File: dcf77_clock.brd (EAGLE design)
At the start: 83.1 x 76.2 mm, 42 parts, among them IC1 7805DT, IC2 ATMEGA48/88/168-AU, J2 DCJ0202, Q1 32.768kHz, Q2 IRLML6244TRPBF, SW1 EC12E_SW, U1 LCD-16X2SILK, U2 DS1307SO8

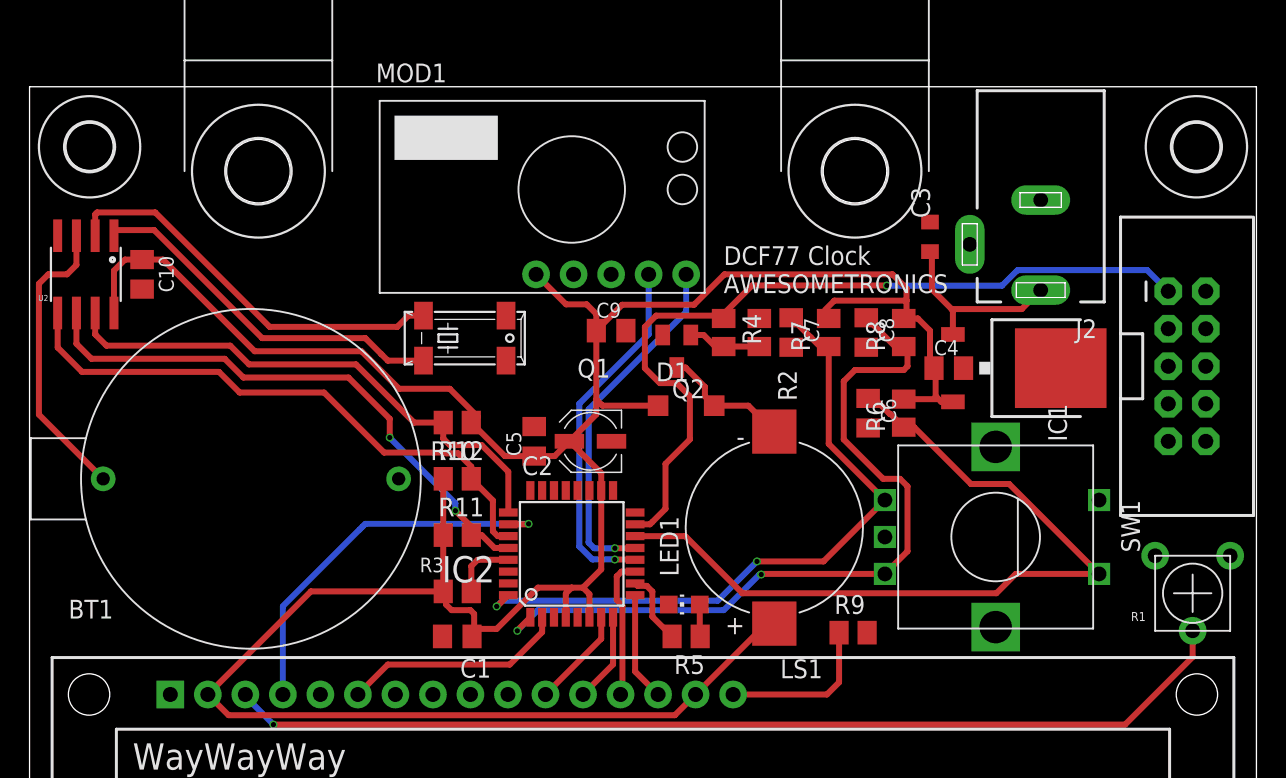
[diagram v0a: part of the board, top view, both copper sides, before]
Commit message: Finish signal and VCC routing
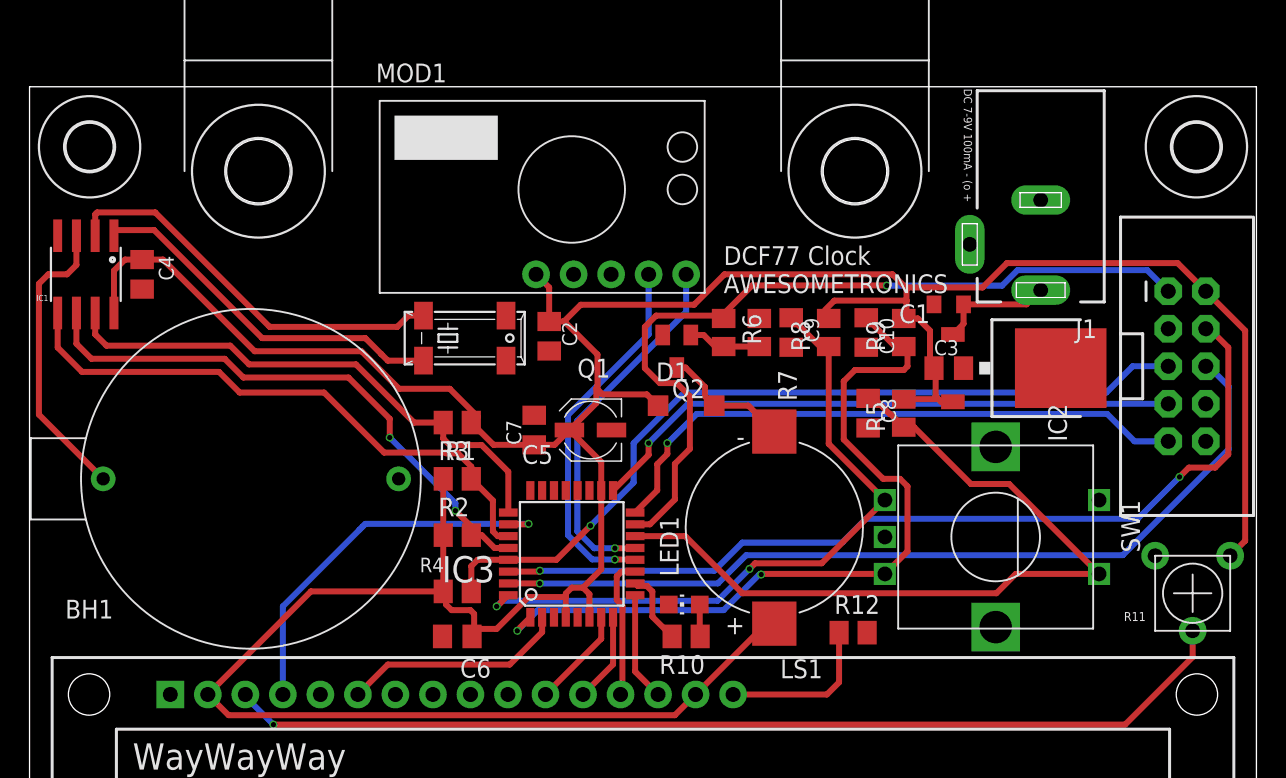
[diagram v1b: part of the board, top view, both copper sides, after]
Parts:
- removed U$1: AVR_SPI_PROG2PTH2, SparkFun:2X5-SHROUDED
- added IC3: ATMEGA48/88/168-AU, atmega8:TQFP32-08
- C1: value 100n -> 0.22uF; device rcl:C0805K -> rcl:SMC_Z
- C2: value 22uF -> 100n; device rcl:UD-4X5,8_NICHICON -> rcl:C0805K
- C3: value 0.22uF -> 100n; device rcl:SMC_Z -> rcl:C0805K
- C5: value 100n -> 22uF; device rcl:C0805K -> rcl:UD-4X5,8_NICHICON
- IC1: value 7805DT -> DS1307SO8; device linear:TO252 -> SparkFun:SO08
- IC2: value ATMEGA48/88/168-AU -> 7805DT; device atmega8:TQFP32-08 -> linear:TO252
- R1: value 10k -> 4.7k; device SparkFun:TRIM_POT_PTH -> rcl:M0805
- R10, R12: value 4.7k -> 100R
- R11: value 4.7k -> 10k; device rcl:M0805 -> SparkFun:TRIM_POT_PTH
- R2, R3: value 10k -> 4.7k
- R4: value 1k -> 10k
- R5, R9: value 100R -> 10k
- R6: value 10k -> 1k
- U1: value LCD-16X2SILK -> AVR_SPI_PROG2PTH2; device SparkFun:LCD-16X2 -> SparkFun:2X5-SHROUDED
- U2: value DS1307SO8 -> LCD-16X2SILK; device SparkFun:SO08 -> SparkFun:LCD-16X2
- moved IC1 63.8 mm to (3.81, 63.5), turned to 180 degrees
- moved U2 57.9 mm to (41.5, 19.6), turned to 0 degrees
- moved C4 55.0 mm to (7.62, 63.5), turned to 270 degrees
- moved U1 52.7 mm to (78.4, 57.3)
- moved R1 51.1 mm to (29.0, 53.5)
- moved R11 49.9 mm to (78.7, 41.9), turned to 180 degrees
- moved C10 49.2 mm to (56.6, 59.6)
- moved HOLD1 40.4 mm to (55.9, 70.5)
- moved HOLD2 40.4 mm to (15.5, 70.5)
- moved C1 40.2 mm to (62.2, 61.5)
- moved IC2 33.1 mm to (67.3, 57.1), turned to 270 degrees
- moved C6 31.7 mm to (29.0, 39.0), turned to 180 degrees
- moved R12 28.7 mm to (55.8, 39.2)
- moved R4 25.1 mm to (29.0, 42.0), turned to 0 degrees
- moved R2 24.6 mm to (29.0, 45.8), turned to 0 degrees
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- renumbered BT1 to BH1, J2 to J1
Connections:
- net DCF77_OUT: now also IC3.12; no longer IC2.12
- net DCF77_SEL: now also IC3.13; no longer IC2.13
- net ENC_A: now also C9.1, IC3.32, R8.1; no longer C7.1, IC2.32, R7.1
- net ENC_B: now also C10.1, IC3.1, R9.1; no longer C8.1, IC2.1, R8.1
- net GND: now also C1.-, C2.2, C3.2, C5.-, IC1.4, IC3.21, IC3.3, IC3.5, R11.3, R12.2, R7.1, U1.10, U1.8, U2.1, U2.5; no longer C1.2, C2.-, C3.-, C5.2, IC1.3, IC2.21, IC2.5, R1.3, R2.1, R9.2, U$1.10, U$1.8, U1.1, U1.5, U2.4
- net ISP_MISO: now also IC3.16, U1.9; no longer IC2.16, U$1.9
- net ISP_MOSI_BUZ_PWM: now also IC3.15, R6.1, U1.1; no longer IC2.15, R4.1, U$1.1
- net ISP_SCK: now also IC3.17, U1.7; no longer IC2.17, U$1.7
- net LCD_DB4: now also IC3.7, U2.11; no longer IC2.7, U1.11
- net LCD_DB5: now also IC3.8, U2.12; no longer IC2.8, U1.12
- net LCD_DB6: now also IC3.11, U2.13; no longer IC2.11, U1.13
- net LCD_DB7: now also IC3.9, U2.14; no longer IC2.9, U1.14
- net LCD_E: now also IC3.2, U2.6; no longer IC2.2, U1.6
- net LCD_RS: now also IC3.26, U2.4; no longer IC2.26, U1.4
- net LED: now also IC3.10, R10.2; no longer IC2.10, R5.2
- net MCU_RX: now also IC3.30, U1.4; no longer IC2.30, U$1.4
- net MCU_TX: now also IC3.31, U1.6; no longer IC2.31, U$1.6
- net N$1: now also C1.+, IC2.1; no longer C3.+, IC1.1
- net N$10: now also IC1.1; no longer U2.1
- net N$11: now also IC1.2; no longer U2.2
- net N$12: now also IC1.3; no longer U2.3
- net N$3: now also R6.2, R7.2; no longer R2.2, R4.2
- net N$4: now also R10.1; no longer R5.1
- net N$7: now also R11.2, U2.3; no longer R1.2, U1.3
- net N$9: now also R12.1, U2.16; no longer R9.1, U1.16
- net RESET: now also IC3.29, R4.2, U1.5; no longer IC2.29, R3.2, U$1.5
- net RTC_SCL: now also IC1.6, IC3.28, R2.2; no longer IC2.28, R11.2, U2.6
- net RTC_SDA: now also IC1.5, IC3.27, R3.2; no longer IC2.27, R12.2, U2.5
- net RTC_SQW: now also IC1.7, IC3.25, R1.2; no longer IC2.25, R10.2, U2.7
- net SW: now also C8.1, IC3.14, R5.1; no longer C6.1, IC2.14, R6.1
- net VCC: now also C2.1, C3.1, C5.+, C6.1, C7.1, IC1.8, IC2.2, IC3.18, IC3.4, IC3.6, R2.1, R4.1, R5.2, R9.2, U2.15, U2.2; no longer C1.1, C10.1, C2.+, C5.1, C9.1, IC1.2, IC2.18, IC2.4, IC2.6, R10.1, R12.1, R6.2, R7.2, U$1.2, U1.15, U2.8
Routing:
- net MCU_RX: track 0.00 -> 61.3 mm, vias 0 -> 2
- net MCU_TX: track 0.00 -> 58.9 mm, vias 0 -> 1
- net RESET: track 4.39 -> 56.1 mm, vias 0 -> 1
- net VCC: track 198.3 -> 240.7 mm
- net ISP_MISO: track 0.00 -> 41.1 mm, vias 0 -> 1
- net ISP_SCK: track 0.00 -> 40.5 mm, vias 0 -> 1
- net N$1: track 12.8 -> 7.96 mm
- net DCF77_OUT: track 24.5 -> 25.2 mm
- net DCF77_SEL: track 24.3 -> 24.9 mm
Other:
- board text added: "DC 7-9V 100mA - (o +"

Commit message: Add BOM
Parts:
- U2: value LCD-16X2SILK -> LCD-16X2UPPERHOLES; device SparkFun:LCD-16X2 -> dcf77:LCD-16X2_UPPER_HOLES
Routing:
- net N$7: track 68.7 -> 68.1 mm

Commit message: Add GND polygon and missing vias
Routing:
- net VCC: track 240.8 -> 241.5 mm
- added copper zone on layer 1, net GND
- added copper zone on layer 16, net GND
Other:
- board text added: "DC 7-9V 100mA"
- board text removed: "DC 7-9V 100mA - (o +"
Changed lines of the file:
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@@
 <dimension x1="10.541" y1="88.9" x2="60.96" y2="88.9" x3="35.7505" y3="97.79" textsize="1.778" layer="1"/>
 <text x="6.985" y="29.972" size="1.778" layer="25">WayWayWay</text>
-<text x="63.246" y="76.073" size="0.5588" layer="25" rot="SR270">DC 7-9V 100mA - (o +</text>
+<text x="63.246" y="76.073" size="0.5588" layer="25" rot="SR270">DC 7-9V 100mA</text>
+<wire x1="63.5" y1="70.1802" x2="63.5" y2="69.9262" width="0.1016" layer="25"/>
+<wire x1="63.373" y1="68.9102" x2="63.5" y2="68.9102" width="0.1016" layer="25"/>
+<wire x1="63.5" y1="68.9102" x2="63.627" y2="68.9102" width="0.1016" layer="25"/>
+<wire x1="63.5" y1="68.9102" x2="63.5" y2="68.7832" width="0.1016" layer="25"/>
+<wire x1="63.5" y1="68.9102" x2="63.5" y2="69.0372" width="0.1016" layer="25"/>
+<wire x1="63.1698" y1="69.4182" x2="63.8048" y2="69.4182" width="0.1016" layer="25" curve="-180"/>
+<circle x="63.5" y="69.4182" radius="0.127" width="0.1016" layer="25"/>
 </plain>
 <attributes>
@@
 <contactref element="C2" pad="2"/>
 <contactref element="C4" pad="2"/>
-<wire x1="63.653" y1="65.532" x2="68.453" y2="68.532" width="0" layer="19" extent="1-1"/>
-<wire x1="61.23" y1="61.468" x2="63.653" y2="65.532" width="0" layer="19" extent="1-1"/>
-<wire x1="63.23" y1="57.15" x2="61.23" y2="61.468" width="0" layer="19" extent="1-1"/>
-<wire x1="56.642" y1="58.563" x2="61.23" y2="61.468" width="0" layer="19" extent="1-1"/>
-<wire x1="51.562" y1="58.563" x2="56.642" y2="58.563" width="0" layer="19" extent="1-1"/>
-<wire x1="49.403" y1="60.513" x2="51.562" y2="58.563" width="0" layer="19" extent="1-1"/>
-<wire x1="56.769" y1="53.102" x2="56.642" y2="58.563" width="0" layer="19" extent="1-1"/>
-<wire x1="69.81" y1="57.15" x2="63.23" y2="57.15" width="0" layer="19" extent="1-1"/>
-<wire x1="42.865" y1="59.393" x2="49.403" y2="60.513" width="0" layer="19" extent="1-1"/>
-<wire x1="36.83" y1="63.5" x2="42.865" y2="59.393" width="0" layer="19" extent="1-1"/>
-<wire x1="35.179" y1="58.309" x2="36.83" y2="63.5" width="0" layer="19" extent="1-1"/>
-<wire x1="34.163" y1="53.959" x2="35.179" y2="58.309" width="0" layer="19" extent="1-1"/>
-<wire x1="39.398" y1="52.959" x2="34.163" y2="53.959" width="0" layer="19" extent="1-1"/>
-<wire x1="36.303" y1="48.8696" x2="39.398" y2="52.959" width="0" layer="19" extent="1-1"/>
-<wire x1="57.905" y1="45.72" x2="56.769" y2="53.102" width="0" layer="19" extent="1-1"/>
-<wire x1="56.703" y1="39.243" x2="57.905" y2="45.72" width="0" layer="19" extent="1-1"/>
-<wire x1="37.103" y1="40.2844" x2="36.303" y2="48.8696" width="0" layer="19" extent="1-1"/>
-<wire x1="35.503" y1="40.2844" x2="37.103" y2="40.2844" width="0" layer="19" extent="1-1"/>
-<wire x1="43.273" y1="41.148" x2="37.103" y2="40.2844" width="0" layer="19" extent="1-1"/>
-<wire x1="27.956" y1="38.989" x2="35.503" y2="40.2844" width="0" layer="19" extent="1-1"/>
-<wire x1="19.689" y1="35.058" x2="27.956" y2="38.989" width="0" layer="19" extent="1-1"/>
-<wire x1="72.405" y1="48.22" x2="69.81" y2="57.15" width="0" layer="19" extent="1-1"/>
-<wire x1="76.2" y1="44.45" x2="72.405" y2="48.22" width="0" layer="19" extent="1-1"/>
-<wire x1="79.629" y1="52.197" x2="72.405" y2="48.22" width="0" layer="19" extent="1-1"/>
-<wire x1="79.629" y1="54.737" x2="79.629" y2="52.197" width="0" layer="19" extent="1-1"/>
-<wire x1="24.986" y1="49.657" x2="34.163" y2="53.959" width="0" layer="19" extent="1-1"/>
-<wire x1="9.529" y1="35.058" x2="19.689" y2="35.058" width="0" layer="19" extent="1-1"/>
-<wire x1="7.62" y1="62.5" x2="24.986" y2="49.657" width="0" layer="19" extent="1-1"/>
-<wire x1="1.905" y1="66.1162" x2="7.62" y2="62.5" width="0" layer="19" extent="1-1"/>
+<polygon width="0.2032" layer="1" isolate="0.2032">
+<vertex x="-2.54" y="80.01"/>
+<vertex x="85.09" y="80.01"/>
+<vertex x="85.09" y="-2.54"/>
+<vertex x="-2.54" y="-2.54"/>
+</polygon>
+<polygon width="0.3048" layer="16" isolate="0.3048">
+<vertex x="-3.81" y="82.55"/>
+<vertex x="88.9" y="82.55"/>
+<vertex x="88.9" y="-8.89"/>
+<vertex x="-12.7" y="-8.89"/>
+<vertex x="-12.7" y="82.55"/>
+</polygon>
+<via x="35.56" y="38.481" extent="1-16" drill="0.35"/>
+<via x="36.576" y="38.481" extent="1-16" drill="0.35"/>
+<via x="33.782" y="36.83" extent="1-16" drill="0.35"/>
+<via x="35.052" y="36.83" extent="1-16" drill="0.35"/>
+<via x="24.13" y="40.64" extent="1-16" drill="0.35"/>
+<via x="25.4" y="40.64" extent="1-16" drill="0.35"/>
+<via x="22.86" y="39.37" extent="1-16" drill="0.35"/>
+<via x="24.257" y="39.37" extent="1-16" drill="0.35"/>
+<via x="25.527" y="39.37" extent="1-16" drill="0.35"/>
+<via x="30.607" y="55.88" extent="1-16" drill="0.35"/>
+<via x="31.75" y="55.88" extent="1-16" drill="0.35"/>
+<via x="33.02" y="55.88" extent="1-16" drill="0.35"/>
+<via x="34.29" y="55.88" extent="1-16" drill="0.35"/>
+<via x="35.56" y="55.88" extent="1-16" drill="0.35"/>
+<via x="39.751" y="51.308" extent="1-16" drill="0.35"/>
+<via x="39.751" y="50.419" extent="1-16" drill="0.35"/>
+<via x="40.894" y="54.229" extent="1-16" drill="0.35"/>
+<via x="48.26" y="56.515" extent="1-16" drill="0.35"/>
+<via x="49.53" y="56.515" extent="1-16" drill="0.35"/>
+<via x="50.8" y="56.515" extent="1-16" drill="0.35"/>
+<via x="52.07" y="56.515" extent="1-16" drill="0.35"/>
+<via x="55.245" y="57.531" extent="1-16" drill="0.35"/>
+<via x="55.372" y="59.563" extent="1-16" drill="0.35"/>
+<via x="60.198" y="61.722" extent="1-16" drill="0.35"/>
+<via x="62.23" y="60.579" extent="1-16" drill="0.35"/>
+<via x="42.291" y="44.704" extent="1-16" drill="0.35"/>
+<via x="43.561" y="44.704" extent="1-16" drill="0.35"/>
+<via x="51.054" y="61.849" extent="1-16" drill="0.35"/>
+<via x="52.578" y="61.849" extent="1-16" drill="0.35"/>
+<via x="33.782" y="50.292" extent="1-16" drill="0.35"/>
+<via x="34.671" y="50.292" extent="1-16" drill="0.35"/>
+<via x="35.433" y="50.292" extent="1-16" drill="0.35"/>
+<via x="57.785" y="51.435" extent="1-16" drill="0.35"/>
+<via x="59.69" y="51.435" extent="1-16" drill="0.35"/>
+<via x="60.452" y="50.673" extent="1-16" drill="0.35"/>
+<via x="61.341" y="49.911" extent="1-16" drill="0.35"/>
+<via x="62.357" y="49.022" extent="1-16" drill="0.35"/>
+<via x="60.96" y="45.72" extent="1-16" drill="0.35"/>
+<via x="63.5" y="45.72" extent="1-16" drill="0.35"/>
+<via x="65.405" y="45.72" extent="1-16" drill="0.35"/>
 </signal>
 <signal name="VCC">
@@
 <wire x1="59.182" y1="55.052" x2="61.402" y2="55.052" width="0.508" layer="1"/>
 <wire x1="61.402" y1="55.052" x2="61.468" y2="55.118" width="0.4064" layer="1"/>
-<wire x1="54.483" y1="61.722" x2="53.848" y2="61.087" width="0.4064" layer="1"/>
+<wire x1="53.848" y1="61.087" x2="54.483" y2="61.722" width="0.4064" layer="1"/>
 <wire x1="60.96" y1="59.69" x2="60.137" y2="60.513" width="0.508" layer="1"/>
 <wire x1="60.137" y1="60.513" x2="59.309" y2="60.513" width="0.4064" layer="1"/>
@@
 <wire x1="82.296" y1="45.466" x2="81.28" y2="44.45" width="0.4064" layer="1"/>
 <wire x1="82.296" y1="59.69" x2="82.296" y2="45.466" width="0.4064" layer="1"/>
-<wire x1="53.848" y1="61.087" x2="54.102" y2="60.513" width="0" layer="19" extent="1-1"/>
+<wire x1="54.102" y1="60.513" x2="53.848" y2="60.767" width="0.3048" layer="1"/>
+<wire x1="53.848" y1="60.767" x2="53.848" y2="61.087" width="0.3048" layer="1"/>
 </signal>
 <signal name="N$1">
@@
 <wire x1="43.688" y1="48.26" x2="43.688" y2="50.673" width="0.4064" layer="1"/>
 <wire x1="43.688" y1="50.673" x2="44.704" y2="51.689" width="0.4064" layer="1"/>
-<wire x1="48.92070625" y1="62.7506" x2="46.99" y2="60.81989375" width="0.4064" layer="1"/>
+<wire x1="46.99" y1="60.81989375" x2="48.92070625" y2="62.7506" width="0.4064" layer="1"/>
 <wire x1="40.9956" y1="46.577" x2="42.005" y2="46.577" width="0.4064" layer="1"/>
-<wire x1="46.99" y1="60.513" x2="46.99" y2="60.81989375" width="0" layer="19" extent="1-1"/>
+<wire x1="46.99" y1="60.513" x2="46.99" y2="60.81989375" width="0.3048" layer="1"/>
 </signal>
 <signal name="ISP_MISO">
@@
 <wire x1="29.083" y1="51.308" x2="29.906" y2="50.485" width="0.4064" layer="1"/>
 </signal>
+<signal name="N$14">
+<via x="42.418" y="37.084" extent="1-16" drill="0.35"/>
+</signal>
+<signal name="N$15">
+<via x="43.942" y="37.084" extent="1-16" drill="0.35"/>
+</signal>
 </signals>

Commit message: Place hidden encoder pins and connect to GND
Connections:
- net GND: now also SW1.GND1, SW1.GND2
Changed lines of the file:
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@@
 <via x="63.5" y="45.72" extent="1-16" drill="0.35"/>
 <via x="65.405" y="45.72" extent="1-16" drill="0.35"/>
+<contactref element="SW1" pad="GND2"/>
+<contactref element="SW1" pad="GND1"/>
 </signal>
 <signal name="VCC">

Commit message: DRC checked
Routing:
- net VCC: track 241.5 -> 242.0 mm
